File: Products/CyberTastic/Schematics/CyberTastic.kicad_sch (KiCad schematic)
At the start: 52 parts, among them J1 USB_C_Receptacle, J2 U.FL, J3 USB_C_Receptacle, J4 Conn_01x04, J5 Conn_01x07, J6 Conn_01x01, J7 Conn_01x01, J8 OledDisplay, J9 Conn_01x04, Q1 AO3401A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

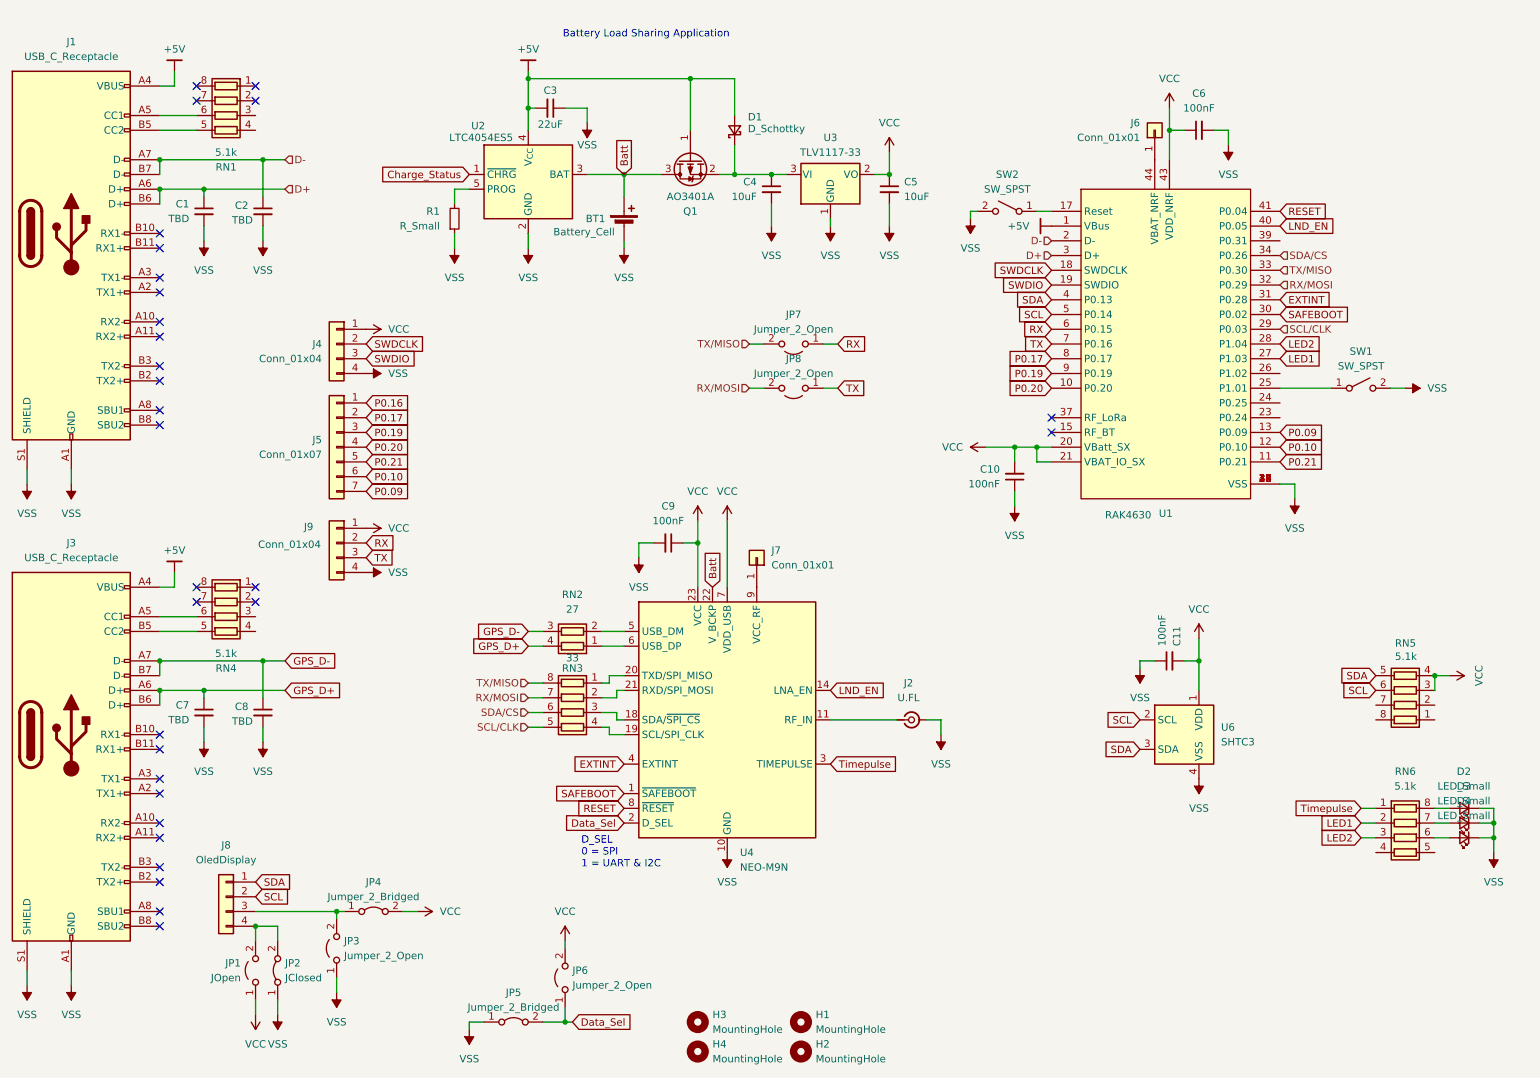
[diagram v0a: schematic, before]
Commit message: Completed V1 Routing
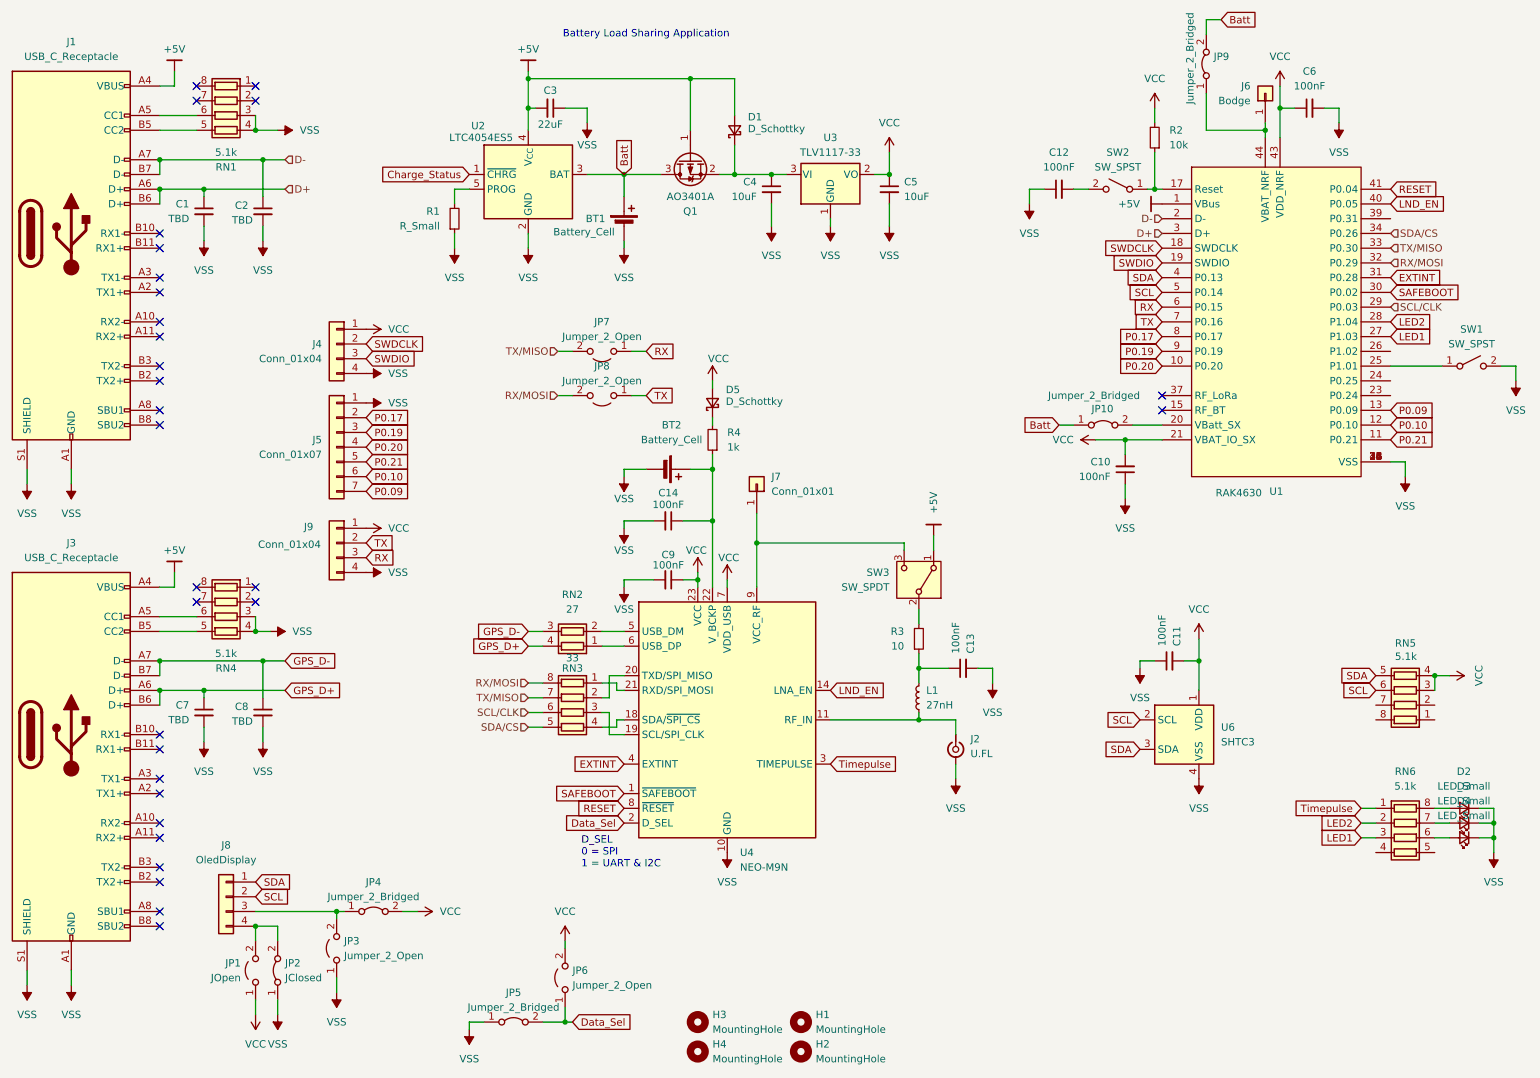
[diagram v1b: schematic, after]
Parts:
- added BT2: Battery_Cell, UE-Battery:SEIKO_ML414H_IV01E, symbol Device:Battery_Cell
- added C12, C13, C14: 100nF, Capacitor_SMD:C_0805_2012Metric, symbol Device:C_Small
- added D5: D_Schottky, Diode_SMD:D_SOD-123, symbol Device:D_Schottky_Small
- added JP10, JP9: Jumper_2_Bridged, Jumper:SolderJumper-2_P1.3mm_Bridged_Pad1.0x1.5mm, symbol Jumper:Jumper_2_Bridged
- added L1: 27nH, Inductor_SMD:L_0805_2012Metric, symbol Device:L_Small
- added R2: 10k, Resistor_SMD:R_0805_2012Metric, symbol Device:R_Small
- added R3: 10, Resistor_SMD:R_0805_2012Metric, symbol Device:R_Small
- added R4: 1k, Resistor_SMD:R_0805_2012Metric, symbol Device:R_Small
- added SW3: SW_SPDT, Button_Switch_SMD:SW_SPDT_PCM12, symbol Switch:SW_SPDT
- J6: value Conn_01x01 -> Bodge
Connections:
- net P0.16 is gone; now on net VSS: J5.1 (Pin_1)
- net +5V: now also SW3.1 (A)
- net Batt: now also JP10.1 (A), JP9.2 (B); no longer U4.22 (V_BCKP)
- net LED1: now also RN6.3 (R3.1); no longer RN6.2 (R2.1)
- net LED2: now also RN6.2 (R2.1); no longer RN6.3 (R3.1)
- net RX: now also J9.3 (Pin_3); no longer J9.2 (Pin_2)
- net RX/MOSI: now also RN3.8 (R1.2); no longer RN3.7 (R2.2)
- net SCL/CLK: now also RN3.6 (R3.2); no longer RN3.5 (R4.2)
- net SDA/CS: now also RN3.5 (R4.2); no longer RN3.6 (R3.2)
- net TX: now also J9.2 (Pin_2); no longer J9.3 (Pin_3)
- net TX/MISO: now also RN3.7 (R2.2); no longer RN3.8 (R1.2)
- net VCC: now also D5.2 (A), R2.2; no longer U1.20 (VBatt_SX)
- net VSS: now also RN1.3 (R3.1), RN1.4 (R4.1), RN4.3 (R3.1), RN4.4 (R4.1), BT2.2 (-), C12.1, C13.2, C14.2; no longer SW2.2 (B)
- net at J6.1 (Pin_1), U1.44 (VBAT_NRF): now also JP9.1 (A)
- net at J2.1 (In), U4.11 (RF_IN): now also L1.1
- net at SW2.1 (A), U1.17 (Reset): now also R2.1
- net at J7.1 (Pin_1), U4.9 (VCC_RF): now also SW3.3 (C)
- net at U4.18 (SDA/~{SPI_CS}): now also RN3.4 (R4.1); no longer RN3.3 (R3.1)
- net at U4.19 (SCL/SPI_CLK): now also RN3.3 (R3.1); no longer RN3.4 (R4.1)
- net at U4.20 (TXD/SPI_MISO): now also RN3.2 (R2.1); no longer RN3.1 (R1.1)
- net at U4.21 (RXD/SPI_MOSI): now also RN3.1 (R1.1); no longer RN3.2 (R2.1)
- new net: C12.2, SW2.2 (B)
- new net: R3.2, SW3.2 (B)
- new net: BT2.1 (+), C14.1, R4.1, U4.22 (V_BCKP)
- new net: D5.1 (K), R4.2
- new net: JP10.2 (B), U1.20 (VBatt_SX)
- new net: C13.1, L1.2, R3.1
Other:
- moved on the sheet: C10, C6, C9, J2, J6, J7, JP7, JP8, SW1, SW2, U1
